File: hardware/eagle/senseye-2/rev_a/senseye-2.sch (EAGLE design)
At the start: 18 parts, among them U1 ADC121S101, U2 ADC121S101, U3 ADC121S101

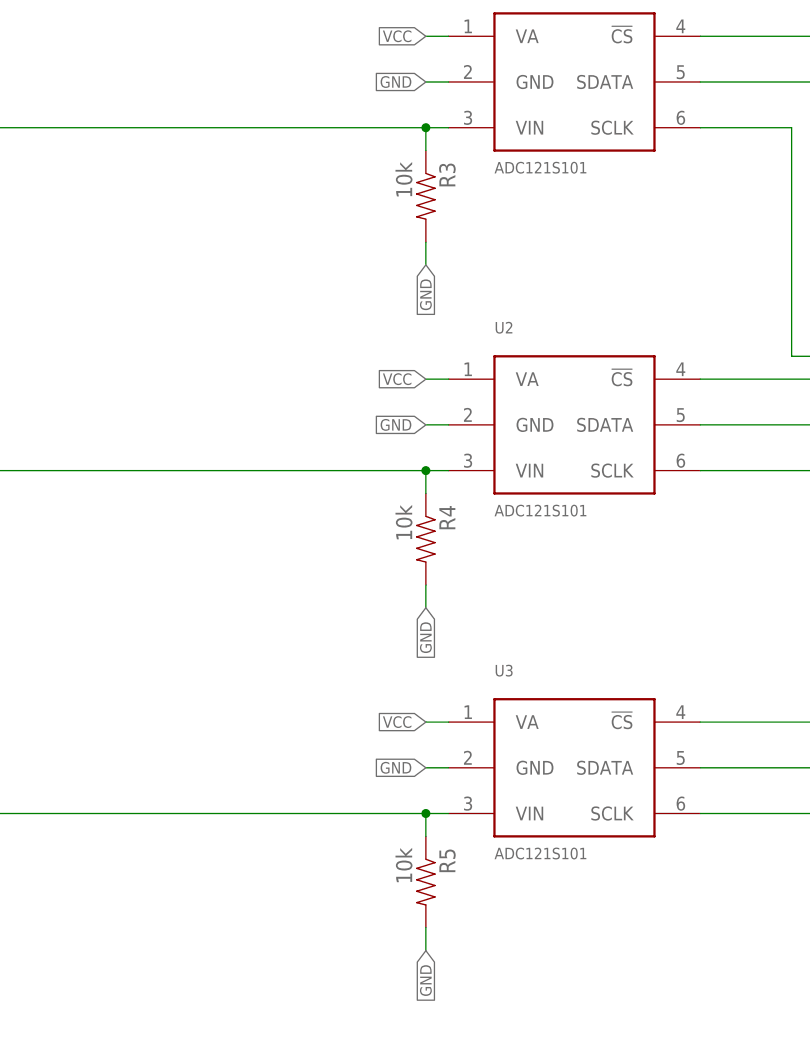
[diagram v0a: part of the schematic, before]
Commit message: updated eagle with 30k resistor
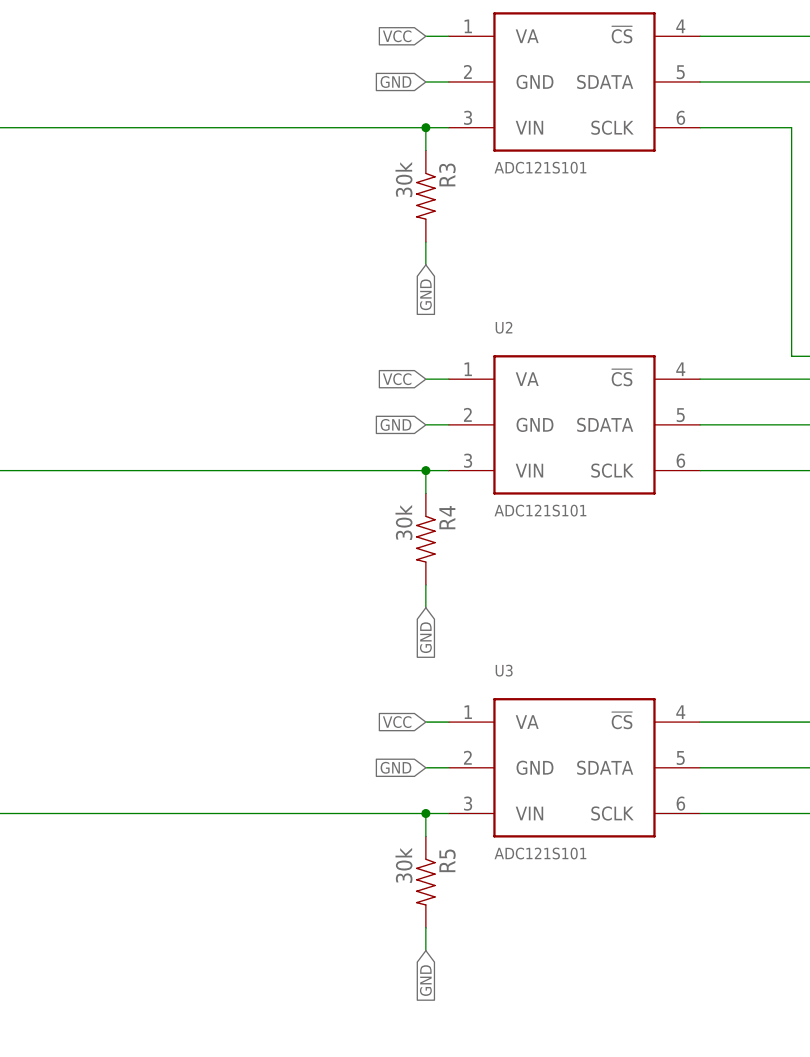
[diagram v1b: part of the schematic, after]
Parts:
- R3, R4, R5: value 10k -> 30k
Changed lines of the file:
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@@
 <?xml version="1.0" encoding="utf-8"?>
 <!DOCTYPE eagle SYSTEM "eagle.dtd">
-<eagle version="6.5.0">
+<eagle version="7.5.0">
 <drawing>
 <settings>
@@
 <part name="D2" library="passives" deviceset="DIODE" device="0603"/>
 <part name="JP3" library="senseye" deviceset="STONYMAN" device=""/>
-<part name="R3" library="passives" deviceset="RESISTOR" device="0402_RES" value="10k"/>
+<part name="R3" library="passives" deviceset="RESISTOR" device="0402_RES" value="30k"/>
 <part name="JP5" library="senseye" deviceset="FH19SC-22S-0.5SH(05)" device=""/>
-<part name="R4" library="passives" deviceset="RESISTOR" device="0402_RES" value="10k"/>
+<part name="R4" library="passives" deviceset="RESISTOR" device="0402_RES" value="30k"/>
 <part name="C1" library="passives" deviceset="CAPACITOR" device="" value="1u"/>
 <part name="C2" library="passives" deviceset="CAPACITOR" device="" value="1u"/>
 <part name="C3" library="passives" deviceset="CAPACITOR" device="" value="1u"/>
 <part name="U3" library="chips" deviceset="ADC121S101" device=""/>
-<part name="R5" library="passives" deviceset="RESISTOR" device="0402_RES" value="10k"/>
+<part name="R5" library="passives" deviceset="RESISTOR" device="0402_RES" value="30k"/>
 <part name="JP4" library="SparkFun-Connectors" deviceset="M02" device="PTH"/>
 <part name="FRAME1" library="frames" deviceset="LETTER_L" device=""/>
